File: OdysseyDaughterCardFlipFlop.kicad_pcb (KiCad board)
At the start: 2 copper layers, 32.6 x 46.6 mm, 16 parts, among them Q1 2N3906, Q2 2N3906, Q3 BC547C, Q4 BC547C, X1 OdysseyDaughterCard

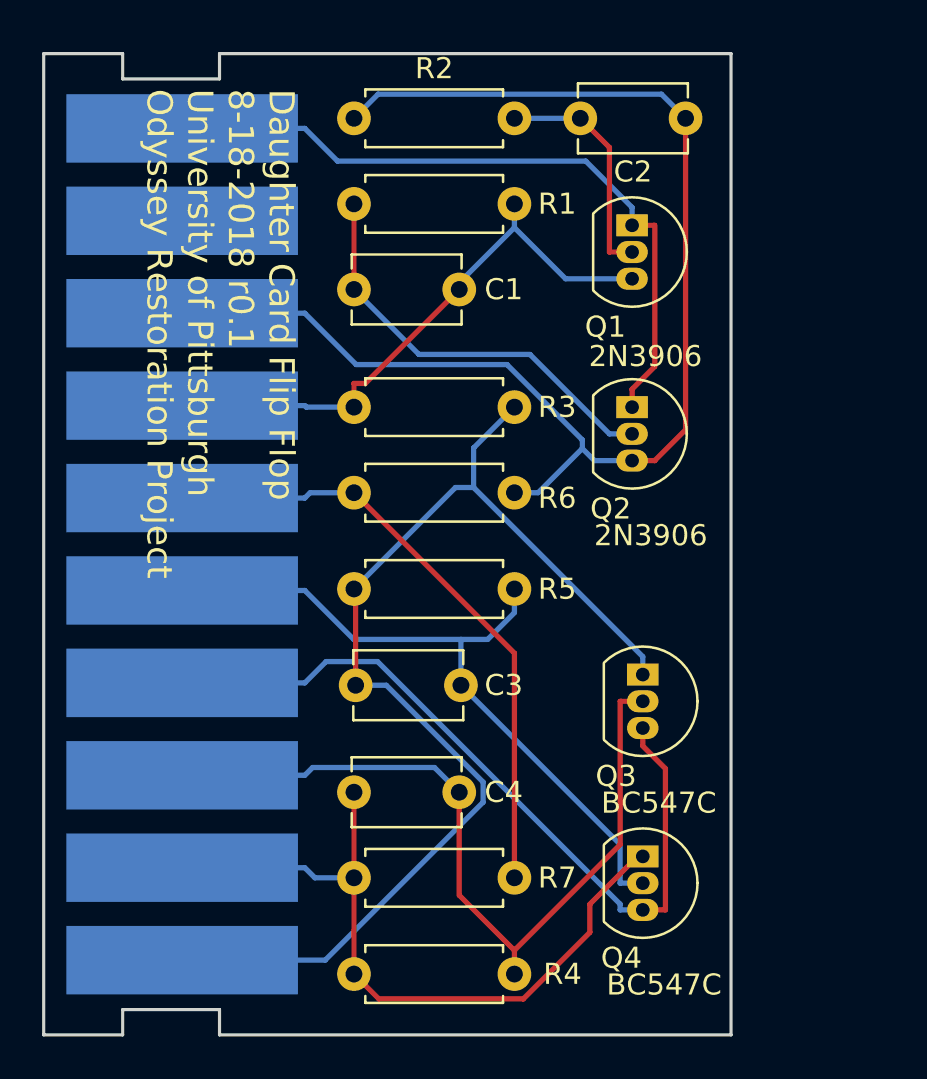
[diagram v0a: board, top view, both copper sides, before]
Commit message: R1.0 Flip-flop add header for extra player generator
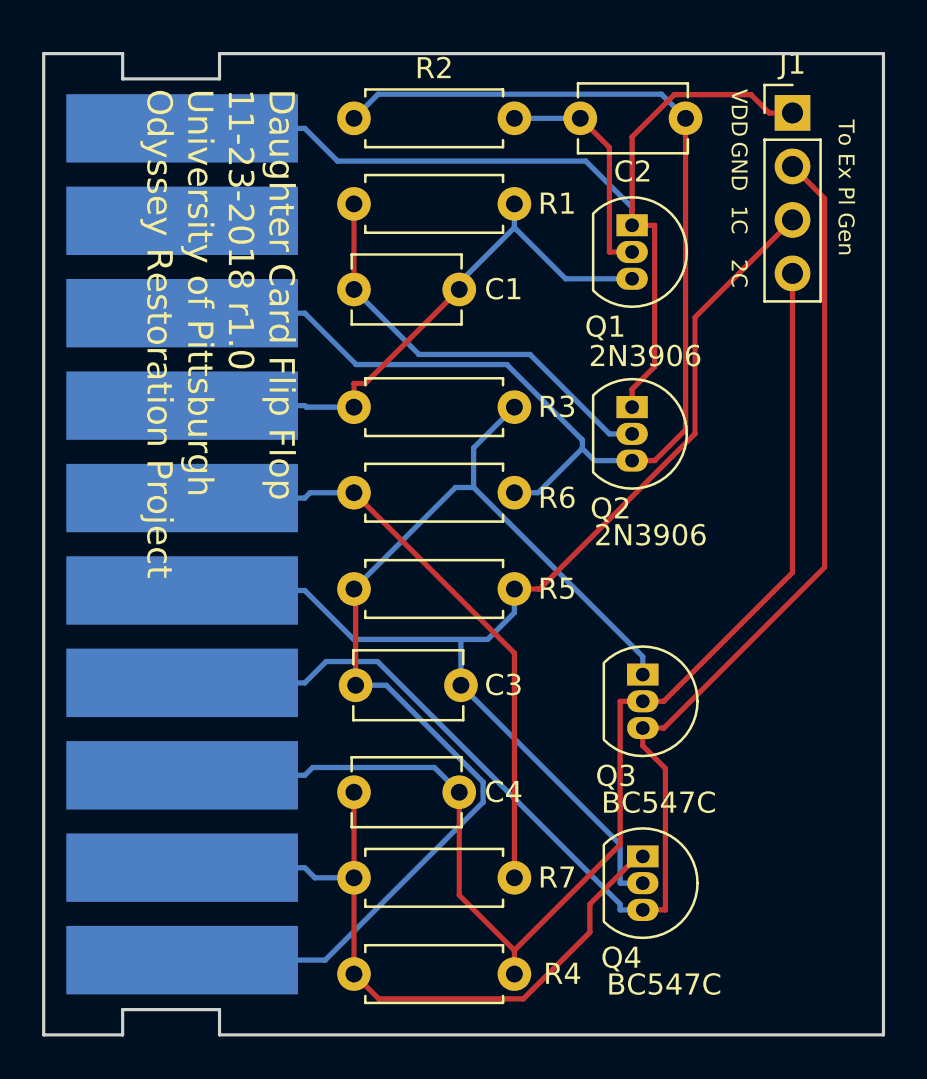
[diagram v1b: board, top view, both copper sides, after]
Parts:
- added J1: Conn_01x04, Connector_PinHeader_2.54mm:PinHeader_1x04_P2.54mm_Vertical, F.Cu at (158.0, 80.5)
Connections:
- X1 pad 9: /Card9 -> (no net)
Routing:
- net GND: track 37.5 -> 69.0 mm
- net /Card3: track 38.5 -> 62.4 mm
- net /Card5: track 34.2 -> 57.9 mm
- net /Card10: track 33.9 -> 46.9 mm
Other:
- board size 32.6 x 46.6 mm -> 39.9 x 46.6 mm
- board text added: "1C"
- board text added: "2C"
- board text added: "Daughter Card Flip Flop 11-23-2018 r1.0 University of Pittsburgh Odyssey Restoration Project"
- board text added: "GND"
- board text added: "To Ex Pl Gen"
- board text added: "VDD"
- board text removed: "Daughter Card Flip Flop 8-18-2018 r0.1 University of Pittsburgh Odyssey Restoration Project"
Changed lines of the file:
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@@
-(kicad_pcb (version 20171130) (host pcbnew "(2017-12-21 revision 23d71cfa9)-makepkg")
+(kicad_pcb (version 20171130) (host pcbnew "(5.0.1)-3")
   (general
     (thickness 1.6)
-    (drawings 13)
-    (tracks 103)
+    (drawings 18)
+    (tracks 121)
     (zones 0)
-    (modules 16)
-    (nets 13)
+    (modules 17)
+    (nets 12)
   )
   (page A4)
   (title_block
     (title "Odyssey Daughter Card Flip Flop")
-    (date 2018-08-18)
-    (rev 0.1)
+    (date 2018-11-23)
+    (rev 1.0)
     (company "University of Pittsburgh - Odyssey Restoration Project")
     (comment 1 "Levi Burner")
@@
     (pad_drill 0.65)
     (pad_to_mask_clearance 0.2)
+    (solder_mask_min_width 0.25)
     (aux_axis_origin 0 0)
     (visible_elements 7FFFFFFF)
@@
       (hpglpennumber 1)
       (hpglpenspeed 20)
-      (hpglpendiameter 15)
+      (hpglpendiameter 15.000000)
       (psnegative false)
       (psa4output false)
@@
       (drillshape 0)
       (scaleselection 1)
-      (outputdirectory gerbers/))
+      (outputdirectory "gerbers/"))
   )
   (net 0 "")
@@
   (net 10 GND)
   (net 11 /Card6)
-  (net 12 /Card9)
   (net_class Default "This is the default net class."
     (clearance 0.2)
@@
     (add_net /Card7)
     (add_net /Card8)
-    (add_net /Card9)
     (add_net GND)
     (add_net "Net-(C1-Pad1)")
@@
     (pad 10 smd rect (at 0 -19.75) (size 11 3.25) (layers B.Cu B.Mask)
       (net 9 /Card10))
-    (pad 9 smd rect (at 0 -15.361112) (size 11 3.25) (layers B.Cu B.Mask)
-      (net 12 /Card9))
+    (pad 9 smd rect (at 0 -15.361112) (size 11 3.25) (layers B.Cu B.Mask))
     (pad 8 smd rect (at 0 -10.972224) (size 11 3.25) (layers B.Cu B.Mask)
       (net 4 /Card8))
@@
     )
   )
-  (gr_line (start 155.067 77.7) (end 155.067 124.3) (layer Edge.Cuts) (width 0.15))
+  (module Connector_PinHeader_2.54mm:PinHeader_1x04_P2.54mm_Vertical (layer F.Cu)
+    (at 157.988 80.518)
+    (descr "Through hole straight pin header, 1x04, 2.54mm pitch, single row")
+    (tags "Through hole pin header THT 1x04 2.54mm single row")
+    (fp_text reference J1 (at 0 -2.33) (layer F.SilkS)
+      (effects (font (size 1 1) (thickness 0.15)))
+    )
+    (fp_text value Conn_01x04 (at 0 9.95) (layer F.Fab)
+      (effects (font (size 1 1) (thickness 0.15)))
+    )
+    (fp_line (start -0.635 -1.27) (end 1.27 -1.27) (layer F.Fab) (width 0.1))
+    (fp_line (start 1.27 -1.27) (end 1.27 8.89) (layer F.Fab) (width 0.1))
+    (fp_line (start 1.27 8.89) (end -1.27 8.89) (layer F.Fab) (width 0.1))
+    (fp_line (start -1.27 8.89) (end -1.27 -0.635) (layer F.Fab) (width 0.1))
+    (fp_line (start -1.27 -0.635) (end -0.635 -1.27) (layer F.Fab) (width 0.1))
+    (fp_line (start -1.33 8.95) (end 1.33 8.95) (layer F.SilkS) (width 0.12))
+    (fp_line (start -1.33 1.27) (end -1.33 8.95) (layer F.SilkS) (width 0.12))
+    (fp_line (start 1.33 1.27) (end 1.33 8.95) (layer F.SilkS) (width 0.12))
+    (fp_line (start -1.33 1.27) (end 1.33 1.27) (layer F.SilkS) (width 0.12))
+    (fp_line (start -1.33 0) (end -1.33 -1.33) (layer F.SilkS) (width 0.12))
+    (fp_line (start -1.33 -1.33) (end 0 -1.33) (layer F.SilkS) (width 0.12))
+    (fp_line (start -1.8 -1.8) (end -1.8 9.4) (layer F.CrtYd) (width 0.05))
+    (fp_line (start -1.8 9.4) (end 1.8 9.4) (layer F.CrtYd) (width 0.05))
+    (fp_line (start 1.8 9.4) (end 1.8 -1.8) (layer F.CrtYd) (width 0.05))
+    (fp_line (start 1.8 -1.8) (end -1.8 -1.8) (layer F.CrtYd) (width 0.05))
+    (fp_text user %R (at 0 3.81 90) (layer F.Fab)
+      (effects (font (size 1 1) (thickness 0.15)))
+    )
+    (pad 1 thru_hole rect (at 0 0) (size 1.7 1.7) (drill 1) (layers *.Cu *.Mask)
+      (net 9 /Card10))
+    (pad 2 thru_hole oval (at 0 2.54) (size 1.7 1.7) (drill 1) (layers *.Cu *.Mask)
+      (net 10 GND))
+    (pad 3 thru_hole oval (at 0 5.08) (size 1.7 1.7) (drill 1) (layers *.Cu *.Mask)
+      (net 5 /Card5))
+    (pad 4 thru_hole oval (at 0 7.62) (size 1.7 1.7) (drill 1) (layers *.Cu *.Mask)
+      (net 8 /Card3))
+    (model ${KISYS3DMOD}/Connector_PinHeader_2.54mm.3dshapes/PinHeader_1x04_P2.54mm_Vertical.wrl
+      (at (xyz 0 0 0))
+      (scale (xyz 1 1 1))
+      (rotate (xyz 0 0 0))
+    )
+  )
+  (gr_text 1C (at 155.448 85.598 270) (layer F.SilkS)
+    (effects (font (size 0.75 0.75) (thickness 0.1)))
+  )
+  (gr_text 2C (at 155.448 88.138 270) (layer F.SilkS)
+    (effects (font (size 0.75 0.75) (thickness 0.1)))
+  )
+  (gr_text GND (at 155.448 83.058 270) (layer F.SilkS)
+    (effects (font (size 0.75 0.75) (thickness 0.1)))
+  )
+  (gr_text VDD (at 155.448 80.518 270) (layer F.SilkS)
+    (effects (font (size 0.75 0.75) (thickness 0.1)))
+  )
+  (gr_text "To Ex Pl Gen" (at 160.528 84.074 270) (layer F.SilkS)
+    (effects (font (size 0.75 0.75) (thickness 0.1)))
+  )
+  (gr_line (start 162.306 77.7) (end 162.306 124.3) (layer Edge.Cuts) (width 0.15))
   (gr_line (start 126.175 77.7) (end 122.425 77.7) (layer Edge.Cuts) (width 0.15))
   (gr_line (start 126.175 78.9) (end 126.175 77.7) (layer Edge.Cuts) (width 0.15))
   (gr_line (start 130.775 78.9) (end 126.175 78.9) (layer Edge.Cuts) (width 0.15))
   (gr_line (start 130.775 77.7) (end 130.775 78.9) (layer Edge.Cuts) (width 0.15))
-  (gr_line (start 155.067 77.7) (end 130.775 77.7) (layer Edge.Cuts) (width 0.15))
-  (gr_line (start 130.775 124.3) (end 155.067 124.3) (layer Edge.Cuts) (width 0.15))
+  (gr_line (start 162.306 77.7) (end 130.775 77.7) (layer Edge.Cuts) (width 0.15))
+  (gr_line (start 130.775 124.3) (end 162.306 124.3) (layer Edge.Cuts) (width 0.15))
   (gr_line (start 130.775 123.1) (end 130.775 124.3) (layer Edge.Cuts) (width 0.15))
   (gr_line (start 126.175 123.1) (end 130.775 123.1) (layer Edge.Cuts) (width 0.15))
   (gr_line (start 126.175 124.3) (end 126.175 123.1) (layer Edge.Cuts) (width 0.15))
   (gr_line (start 122.425 124.3) (end 126.175 124.3) (layer Edge.Cuts) (width 0.15))
-  (gr_text "Daughter Card Flip Flop\n8-18-2018 r0.1\nUniversity of Pittsburgh\nOdyssey Restoration Project" (at 130.81 79.375 -90) (layer F.SilkS)
+  (gr_text "Daughter Card Flip Flop\n11-23-2018 r1.0\nUniversity of Pittsburgh\nOdyssey Restoration Project" (at 130.81 79.375 -90) (layer F.SilkS)
     (effects (font (size 1.2 1.2) (thickness 0.2)) (justify left))
   )
@@
   (segment (start 137.1502 105.5193) (end 134.8253 103.1944) (width 0.25) (layer B.Cu) (net 5))
   (segment (start 142.24 105.5193) (end 137.1502 105.5193) (width 0.25) (layer B.Cu) (net 5))
+  (segment (start 145.91137 103.124) (end 144.78 103.124) (width 0.25) (layer F.Cu) (net 5))
+  (segment (start 145.98371 103.124) (end 145.91137 103.124) (width 0.25) (layer F.Cu) (net 5))
+  (segment (start 153.358009 95.749701) (end 145.98371 103.124) (width 0.25) (layer F.Cu) (net 5))
+  (segment (start 153.35801 90.22799) (end 153.358009 95.749701) (width 0.25) (layer F.Cu) (net 5))
+  (segment (start 157.988 85.598) (end 153.35801 90.22799) (width 0.25) (layer F.Cu) (net 5))
   (segment (start 137.24 103.204) (end 137.24 107.696) (width 0.25) (layer F.Cu) (net 6))
   (segment (start 137.16 103.124) (end 137.24 103.204) (width 0.25) (layer F.Cu) (net 6))
@@
   (segment (start 142.16 112.776) (end 140.9855 111.6015) (width 0.25) (layer B.Cu) (net 8))
   (segment (start 129 111.9722) (end 134.8253 111.9722) (width 0.25) (layer B.Cu) (net 8))
+  (segment (start 151.876 108.458) (end 150.876 108.458) (width 0.25) (layer F.Cu) (net 8))
+  (segment (start 157.988 102.346) (end 151.876 108.458) (width 0.25) (layer F.Cu) (net 8))
+  (segment (start 157.988 88.138) (end 157.988 102.346) (width 0.25) (layer F.Cu) (net 8))
   (segment (start 151.4433 92.5624) (end 151.4433 85.852) (width 0.25) (layer F.Cu) (net 9))
   (segment (start 150.368 93.6377) (end 151.4433 92.5624) (width 0.25) (layer F.Cu) (net 9))
@@
   (segment (start 150.368 85.852) (end 150.368 85.0017) (width 0.25) (layer B.Cu) (net 9))
   (segment (start 129 81.25) (end 134.8253 81.25) (width 0.25) (layer B.Cu) (net 9))
+  (segment (start 150.368 85.077) (end 150.368 85.852) (width 0.25) (layer F.Cu) (net 9))
+  (segment (start 150.368 81.646998) (end 150.368 85.077) (width 0.25) (layer F.Cu) (net 9))
+  (segment (start 152.367999 79.646999) (end 150.368 81.646998) (width 0.25) (layer F.Cu) (net 9))
+  (segment (start 156.016999 79.646999) (end 152.367999 79.646999) (width 0.25) (layer F.Cu) (net 9))
+  (segment (start 156.888 80.518) (end 156.016999 79.646999) (width 0.25) (layer F.Cu) (net 9))
+  (segment (start 157.988 80.518) (end 156.888 80.518) (width 0.25) (layer F.Cu) (net 9))
   (segment (start 151.9513 111.6536) (end 150.876 110.5783) (width 0.25) (layer F.Cu) (net 10))
   (segment (start 151.9513 118.364) (end 151.9513 111.6536) (width 0.25) (layer F.Cu) (net 10))
@@
   (segment (start 129 107.5833) (end 134.8253 107.5833) (width 0.25) (layer B.Cu) (net 10))
   (segment (start 150.876 118.364) (end 149.8007 118.364) (width 0.25) (layer B.Cu) (net 10))
+  (segment (start 151.876 109.728) (end 150.876 109.728) (width 0.25) (layer F.Cu) (net 10))
+  (segment (start 159.512 102.092) (end 151.876 109.728) (width 0.25) (layer F.Cu) (net 10))
+  (segment (start 157.988 83.058) (end 159.512 84.582) (width 0.25) (layer F.Cu) (net 10))
+  (segment (start 159.512 84.582) (end 159.512 102.092) (width 0.25) (layer F.Cu) (net 10))
   (segment (start 144.78 106.172) (end 137.16 98.552) (width 0.25) (layer F.Cu) (net 11))
   (segment (start 144.78 116.84) (end 144.78 106.172) (width 0.25) (layer F.Cu) (net 11))

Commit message: Update to R1.1, remove power output for extra player generator
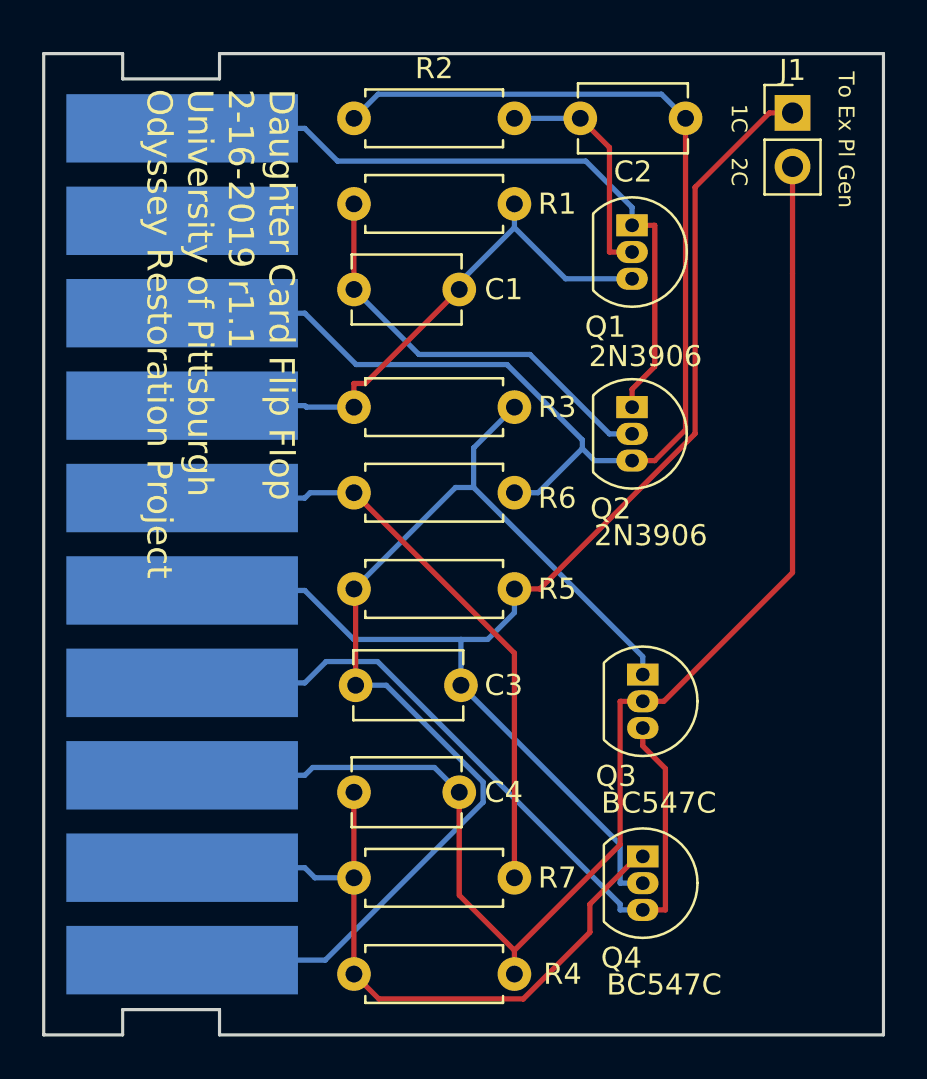
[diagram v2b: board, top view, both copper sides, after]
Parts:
- J1: value Conn_01x04 -> Conn_01x02; footprint Connector_PinHeader_2.54mm:PinHeader_1x04_P2.54mm_Vertical -> Connector_PinHeader_2.54mm:PinHeader_1x02_P2.54mm_Vertical
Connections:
- J1 pad 1: /Card10 -> /Card5
- J1 pad 2: GND -> /Card3
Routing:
- net GND: track 69.0 -> 37.5 mm
- net /Card10: track 46.9 -> 33.9 mm
- net /Card5: track 57.9 -> 63.6 mm
- net /Card3: track 62.4 -> 67.4 mm
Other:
- board text added: "Daughter Card Flip Flop 2-16-2019 r1.1 University of Pittsburgh Odyssey Restoration Project"
- board text removed: "Daughter Card Flip Flop 11-23-2018 r1.0 University of Pittsburgh Odyssey Restoration Project"
- board text removed: "GND"
- board text removed: "VDD"
